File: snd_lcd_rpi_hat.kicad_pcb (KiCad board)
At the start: 2 copper layers, 65 x 56 mm, 40 parts, among them J1 Conn_01x03, J10 Conn_01x02, J11 Conn_01x02, J12 Conn_01x02, J2 Conn_01x03, J3 Conn_01x02, J4 Conn_01x02, J5 Conn_01x03, J6 Conn_01x03, J7 RPi_GPIO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

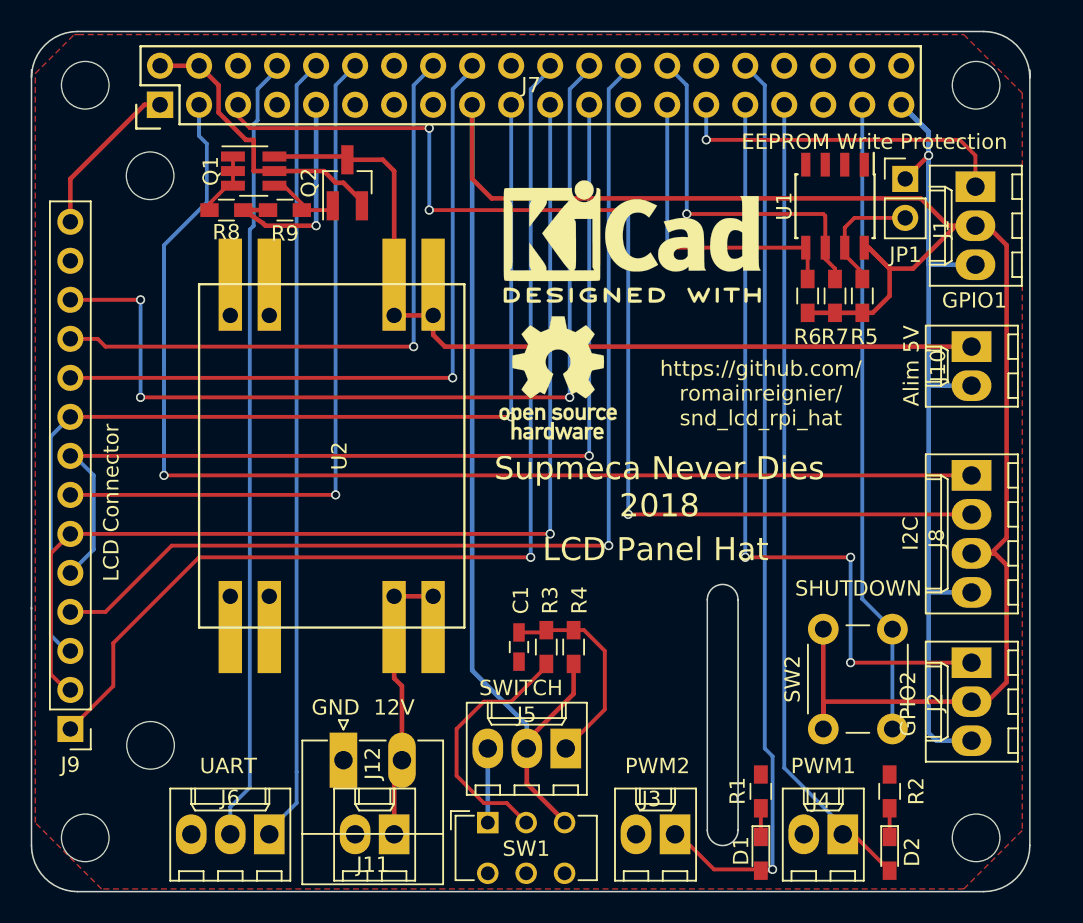
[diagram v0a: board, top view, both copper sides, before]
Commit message: Add missing track between Raspberry Pi header and the switch
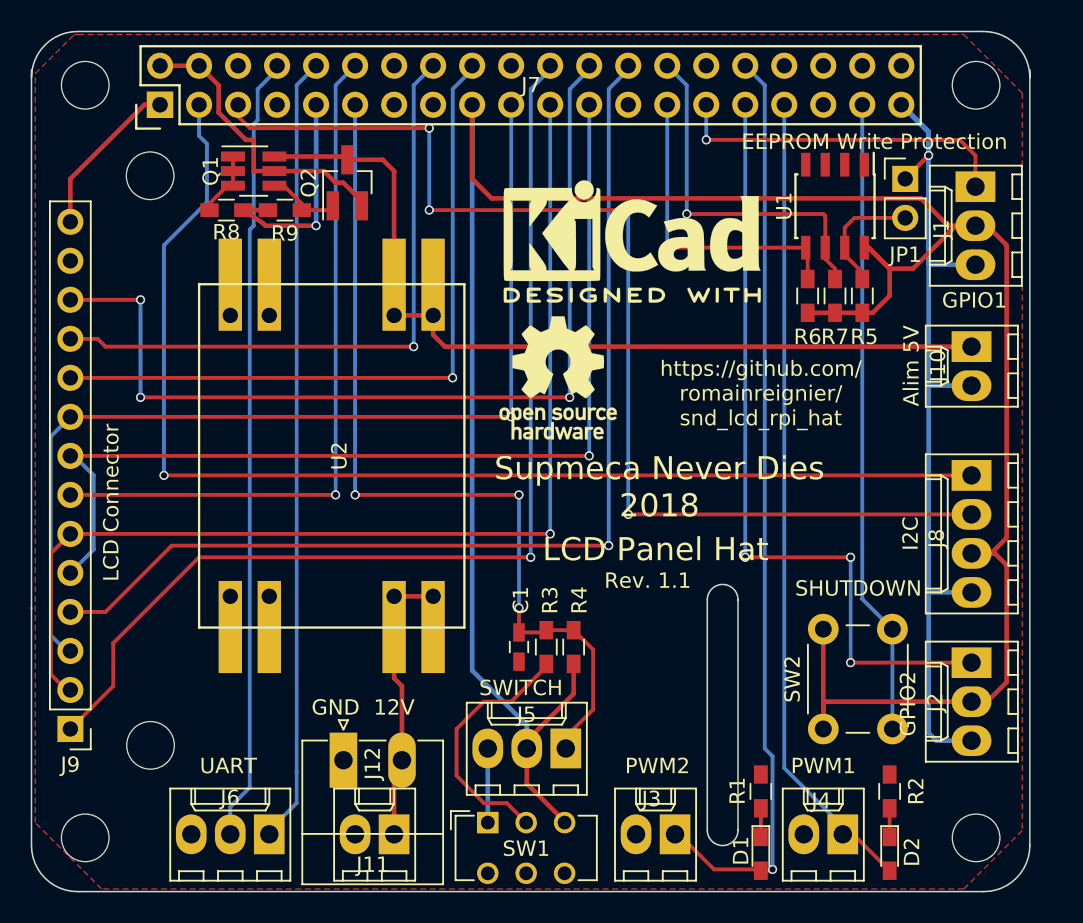
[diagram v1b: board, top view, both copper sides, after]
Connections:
- J7 pad 11: Net-(J7-Pad11) -> /SWITCH
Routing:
- net /SWITCH: track 13.6 -> 57.6 mm, vias 0 -> 3
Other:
- board text added: "Rev. 1.1"
